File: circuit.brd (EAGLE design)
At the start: 83.8 x 100 mm, 12 parts, among them IC1 MEGA8-P

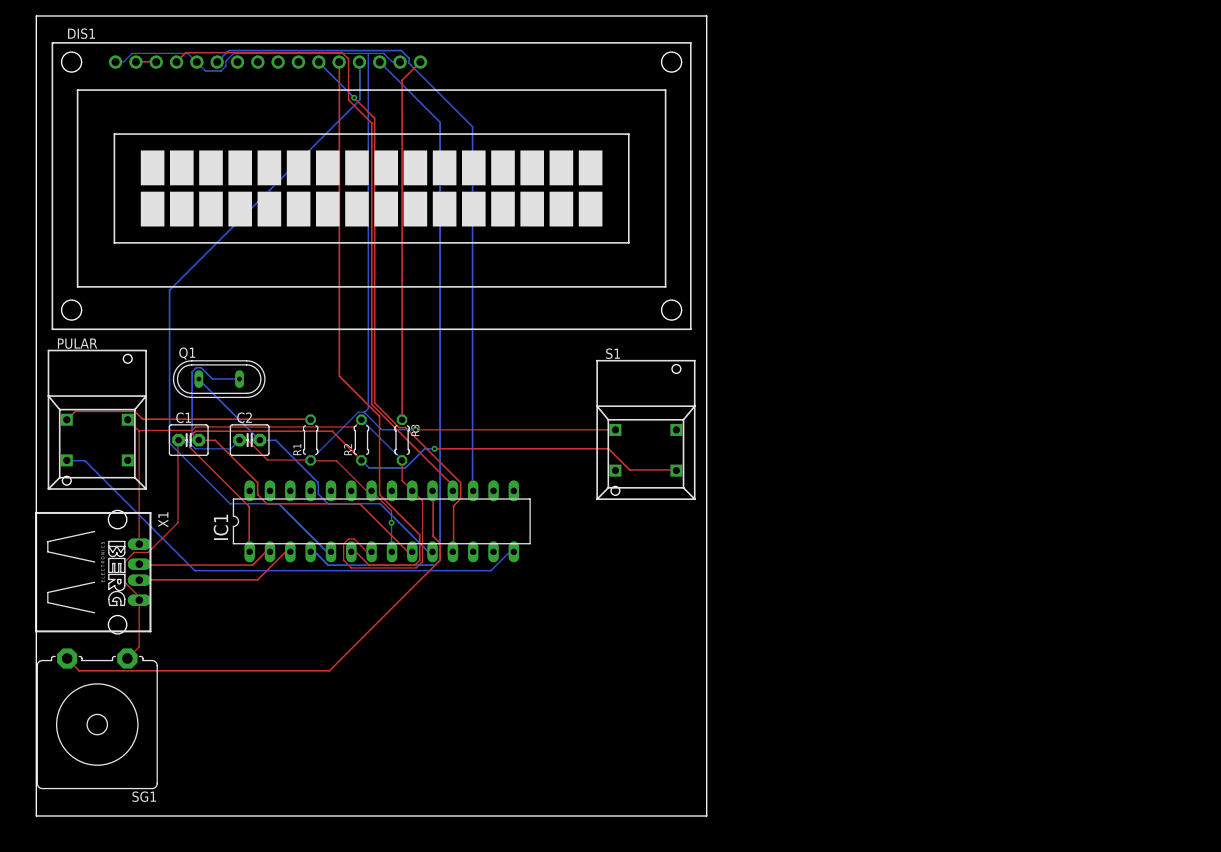
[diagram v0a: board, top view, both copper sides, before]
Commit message: Atualização das trilhas com os modelos 3D
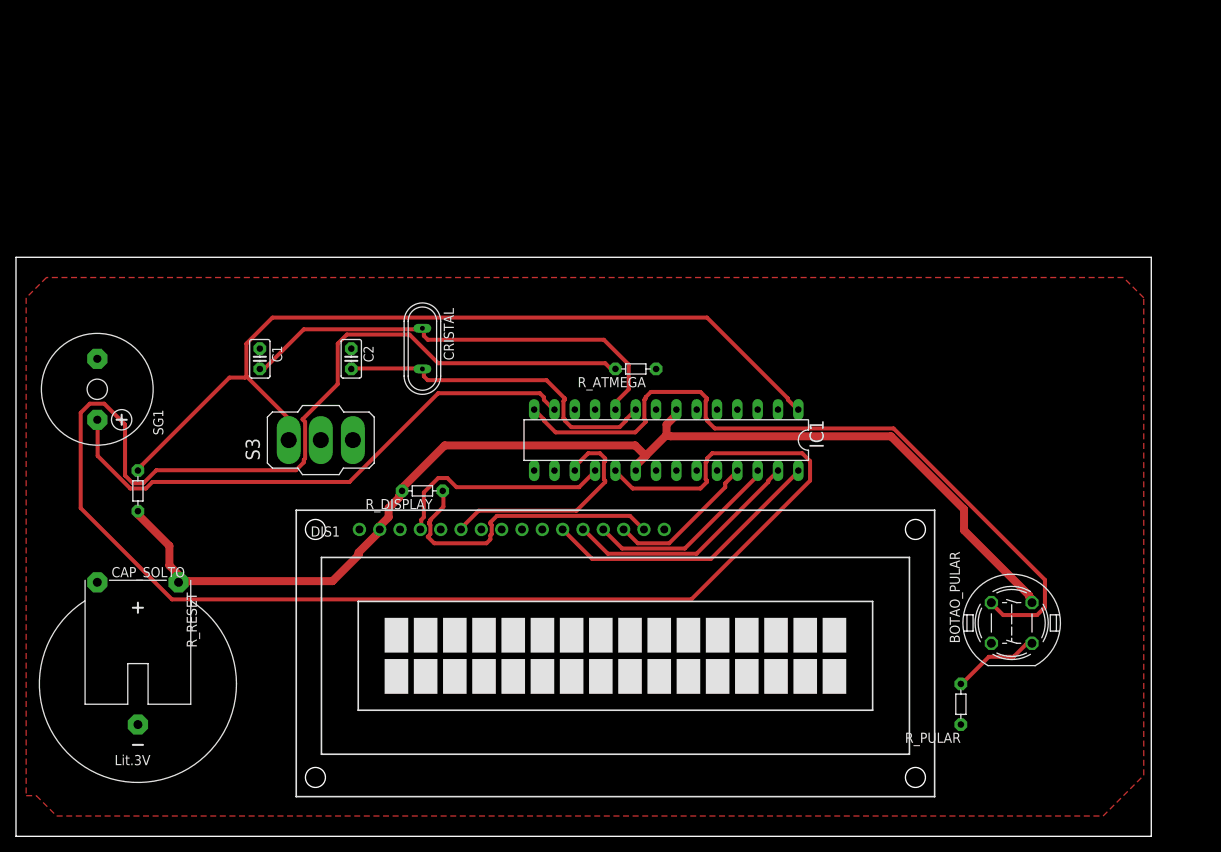
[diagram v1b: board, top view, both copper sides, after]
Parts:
- removed PULAR, S1: 5501, switch:5501
- removed Q1: (no value), special:QS
- removed R1, R2, R3: (no value), rcl:0204/5
- removed X1: (no value), con-berg:PN87520
- added BOTAO_PULAR: DT6, switch-misc:DT6
- added CAP_SOLTO: CR2430H, battery:CR2430H
- added CRISTAL: (no value), special:QS
- added R_ATMEGA, R_DISPLAY, R_PULAR: (no value), discrete:R-5
- added R_RESET: 10k, discrete:R-5
- added S3: (no value), switch:320-916
- C1, C2: device capacitor-wima:C2.5-4 -> capacitor-wima:C2.5-2
- IC1: value MEGA8-P -> ATMEGA328-20P; device avr-7:DIL28-3 -> atmega328:DIL28-3
- SG1: value B/C11L -> F/CM12P; device buzzer:B/C11L -> buzzer:F/CM12P
- moved DIS1 65.9 mm to (72.4, 20.3)
- moved SG1 41.9 mm to (7.62, 53.3), turned to 270 degrees
- moved IC1 37.0 mm to (78.7, 47.0), turned to 180 degrees
- moved C2 16.3 mm to (39.4, 57.1), turned to 270 degrees
- moved C1 13.5 mm to (27.9, 57.1), turned to 270 degrees
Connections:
- removed net N$10 (its old number): DIS1.11, IC1.11
- removed net N$14: DIS1.16, R3.1
- removed net N$2: DIS1.13, IC1.5
- removed net N$3: C2.2, IC1.10, Q1.1
- removed net N$9 (its old number): IC1.1, R2.1, S1.NO
- new net N$11: DIS1.11, IC1.28
- new net N$13: DIS1.13, IC1.26
- new net N$19: BOTAO_PULAR.2, IC1.14
- new net N$8: DIS1.15, R_DISPLAY.1
- net GND: now also CAP_SOLTO.-, DIS1.16, DIS1.3, R_ATMEGA.1, R_PULAR.1, S3.2, SG1.-; no longer DIS1.15, R1.1, S1.1B, SG1.1, X1.4
- net N$1: now also IC1.13, SG1.+; no longer DIS1.14, IC1.4
- net N$12: now also DIS1.12, IC1.27; no longer IC1.19, SG1.2
- net N$15: now also DIS1.14, IC1.25; no longer DIS1.2, DIS1.3
- net N$16: now also IC1.16; no longer IC1.2, X1.2
- net N$17: now also BOTAO_PULAR.4, R_PULAR.2; no longer IC1.3, X1.3
- net N$4: now also IC1.1, R_RESET.1, S3.1; no longer C1.2, IC1.9, Q1.2
- net N$5: now also C1.2, CRISTAL.1, IC1.10; no longer DIS1.12, IC1.6
- net N$6: now also C2.2, CRISTAL.2, IC1.9; no longer PULAR.1B, R1.2
- net N$7: now also IC1.19, R_ATMEGA.2; no longer IC1.14, PULAR.NC
- net VCC: now also BOTAO_PULAR.3, CAP_SOLTO.+, DIS1.2, R_DISPLAY.2, R_RESET.2; no longer PULAR.1A, R2.2, R3.2, X1.1
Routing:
- net GND: track 194.1 -> 0.00 mm, vias 2 -> 0
- net N$7: track 62.6 -> 236.9 mm
- net N$19: track 0.00 -> 91.9 mm
- net N$2: track 83.3 -> 0.00 mm
- net N$9 (its old number): track 82.6 -> 0.00 mm, vias 1 -> 0
- net N$10 (its old number): track 69.5 -> 0.00 mm, vias 1 -> 0
- net VCC: track 82.5 -> 144.8 mm
- net N$4: track 48.9 -> 108.0 mm
- net N$10: track 82.4 -> 29.0 mm
- net N$9: track 81.7 -> 28.3 mm
- net N$14: track 45.7 -> 0.00 mm
- net N$3: track 39.0 -> 0.00 mm
- net N$8: track 0.00 -> 37.6 mm
- net N$11: track 0.00 -> 35.7 mm
- net N$12: track 62.1 -> 30.1 mm
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- added copper zone on layer 1, net GND
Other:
- board size 83.8 x 100 mm -> 141.9 x 72.4 mm

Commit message: Versão final do circuito
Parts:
- removed CAP_SOLTO: CR2430H, battery:CR2430H
- removed R_ATMEGA, R_DISPLAY, R_PULAR: (no value), discrete:R-5
- removed R_RESET: 10k, discrete:R-5
- added G1: CR2032H, battery:CR2032H
- added R1, R2, R3, R4: (no value), rcl:0204/7
- C1, C2: device capacitor-wima:C2.5-2 -> capacitor-wima:C5B3.5
- moved S3 103.2 mm to (133.3, 80.0), turned to 0 degrees
- moved C1 74.1 mm to (101.6, 49.5), turned to 180 degrees
- moved C2 63.8 mm to (101.6, 43.2), turned to 180 degrees
- moved IC1 56.7 mm to (24.1, 62.2), turned to 270 degrees
- moved DIS1 56.6 mm to (81.3, 76.2)
- moved BOTAO_PULAR 46.0 mm to (80.0, 43.2), turned to 180 degrees
- moved SG1 40.9 mm to (25.4, 90.2), turned to 90 degrees
- moved CRISTAL 34.3 mm to (14.0, 57.1), turned to 90 degrees
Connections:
- removed net N$7: IC1.19, R_ATMEGA.2
- removed net N$8: DIS1.15, R_DISPLAY.1
- new net N$2: IC1.19, R2.1
- new net N$3: DIS1.15, R3.1
- net GND: now also G1.-, R1.2, R2.2; no longer CAP_SOLTO.-, R_ATMEGA.1, R_PULAR.1
- net N$17: now also R1.1; no longer R_PULAR.2
- net N$4: now also R4.2; no longer R_RESET.1
- net VCC: now also G1.+, R3.2, R4.1; no longer CAP_SOLTO.+, R_DISPLAY.2, R_RESET.2
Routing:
- net N$7: track 236.9 -> 0.00 mm
- net VCC: track 144.8 -> 317.4 mm
- net N$5: track 56.8 -> 197.9 mm
- net N$4: track 108.0 -> 201.0 mm
- net N$10: track 29.0 -> 115.5 mm
- net N$9: track 28.3 -> 113.7 mm
- net N$6: track 41.8 -> 111.8 mm
- net N$3: track 0.00 -> 55.0 mm
- net N$15: track 19.0 -> 67.6 mm
- net N$2: track 0.00 -> 45.1 mm
- net N$13: track 24.7 -> 65.0 mm
- net N$8: track 37.6 -> 0.00 mm
- net N$19: track 91.9 -> 60.4 mm
- net N$12: track 30.1 -> 60.8 mm
- net N$11: track 35.7 -> 56.7 mm
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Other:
- board size 141.9 x 72.4 mm -> 137.1 x 67 mm
